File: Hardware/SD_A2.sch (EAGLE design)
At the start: 31 parts, among them IC1 74LS245N, IC2 LM317, IC3 2716 / 2732, IC4 XC9572XL

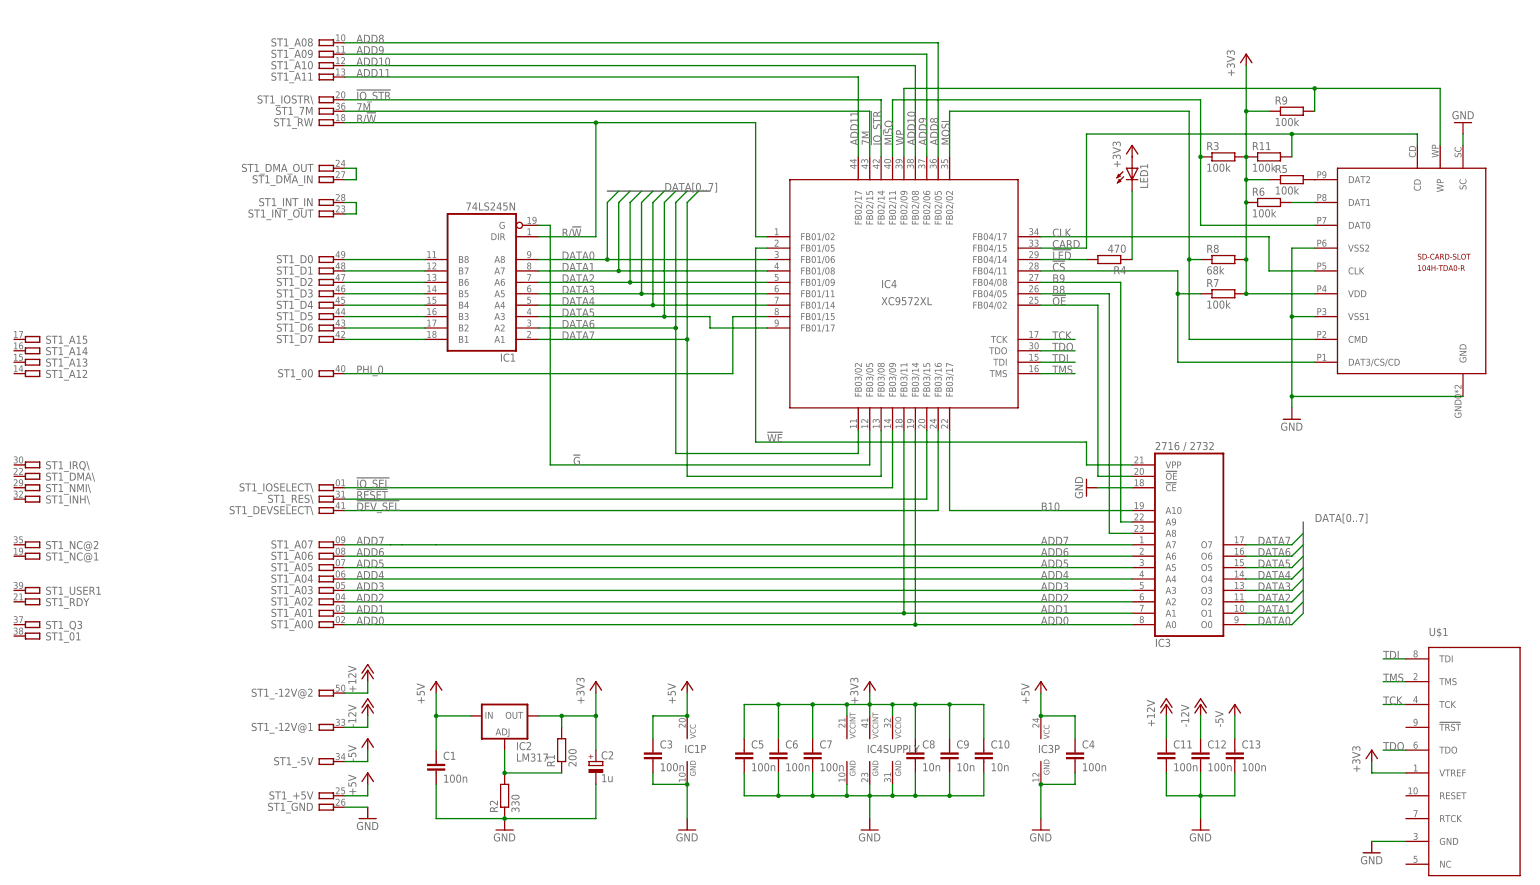
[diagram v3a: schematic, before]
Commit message: EEPROM as SMD
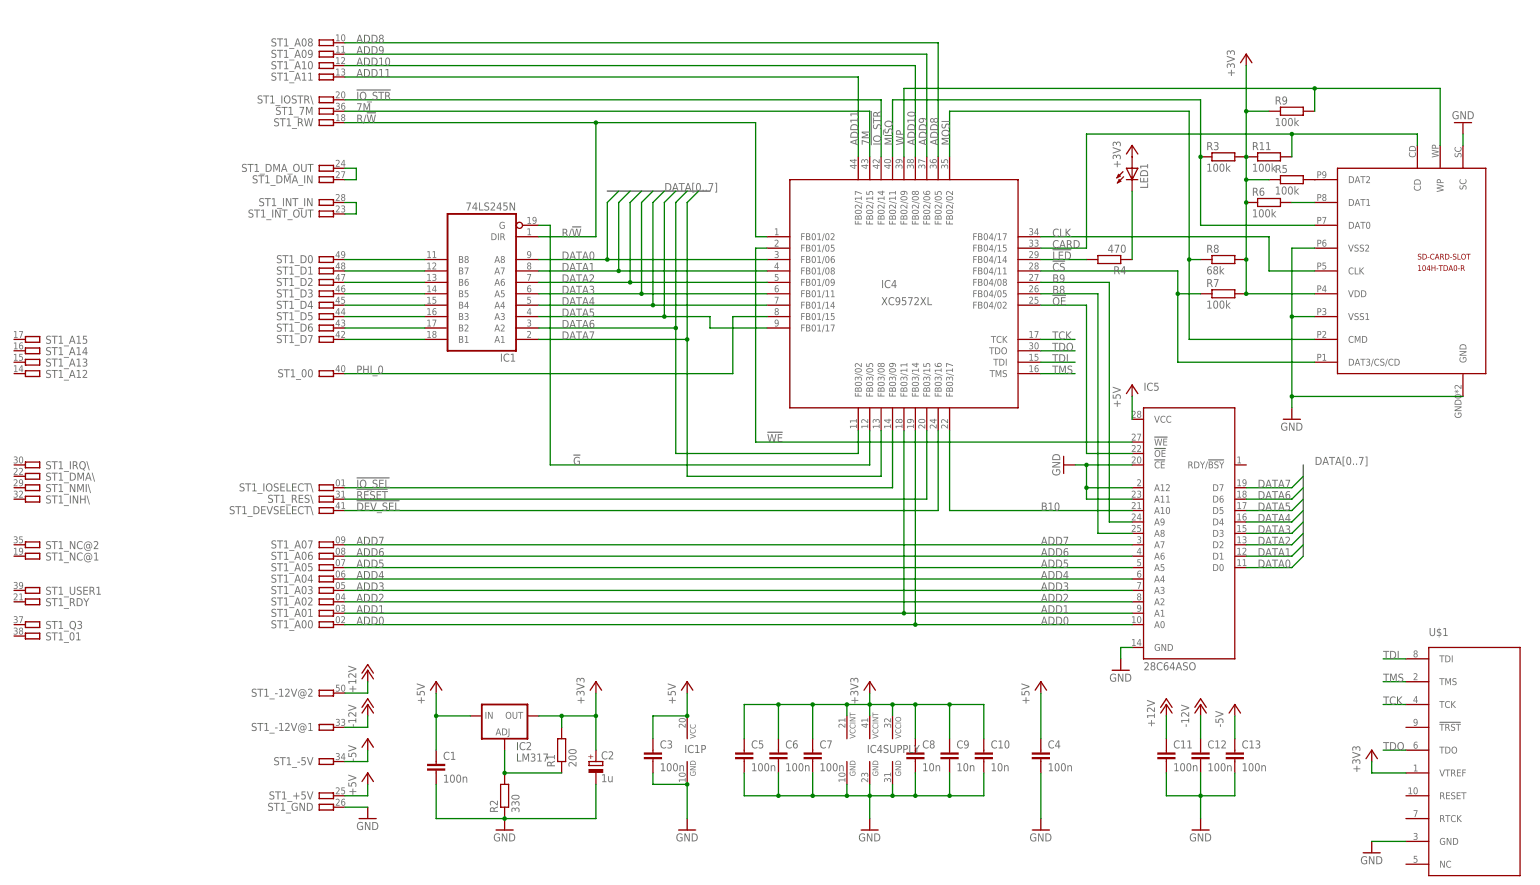
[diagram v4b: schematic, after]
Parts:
- removed IC3: 2716 / 2732, memory:2716
- added IC5: 28C64ASO, microchip:28C64ASO
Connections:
- net N$10 renamed D6
- net N$11 renamed D5
- net N$14 renamed D4
- net N$15 renamed D3
- net N$16 renamed D2
- net N$17 renamed D1
- net N$7 renamed D0
- net N$8 renamed D7
- net !OE: now also IC5.!OE; no longer IC3A.!OE
- net !WE: now also IC5.!WE; no longer IC3A.VPP
- net +5V: now also IC5.VCC; no longer IC3P.VCC
- net ADD0: now also IC5.A0; no longer IC3A.A0
- net ADD1: now also IC5.A1; no longer IC3A.A1
- net ADD2: now also IC5.A2; no longer IC3A.A2
- net ADD3: now also IC5.A3; no longer IC3A.A3
- net ADD4: now also IC5.A4; no longer IC3A.A4
- net ADD5: now also IC5.A5; no longer IC3A.A5
- net ADD6: now also IC5.A6; no longer IC3A.A6
- net ADD7: now also IC5.A7; no longer IC3A.A7
- net B10: now also IC5.A10; no longer IC3A.A10
- net B8: now also IC5.A8; no longer IC3A.A8
- net B9: now also IC5.A9; no longer IC3A.A9
- net DATA0: now also IC5.D0; no longer IC3A.O0
- net DATA1: now also IC5.D1; no longer IC3A.O1
- net DATA2: now also IC5.D2; no longer IC3A.O2
- net DATA3: now also IC5.D3; no longer IC3A.O3
- net DATA4: now also IC5.D4; no longer IC3A.O4
- net DATA5: now also IC5.D5; no longer IC3A.O5
- net DATA6: now also IC5.D6; no longer IC3A.O6
- net DATA7: now also IC5.D7; no longer IC3A.O7
- net GND: now also IC5.!CE, IC5.A11, IC5.A12, IC5.GND; no longer IC3A.!CE, IC3P.GND
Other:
- moved on the sheet: C4

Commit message: Resistor network added
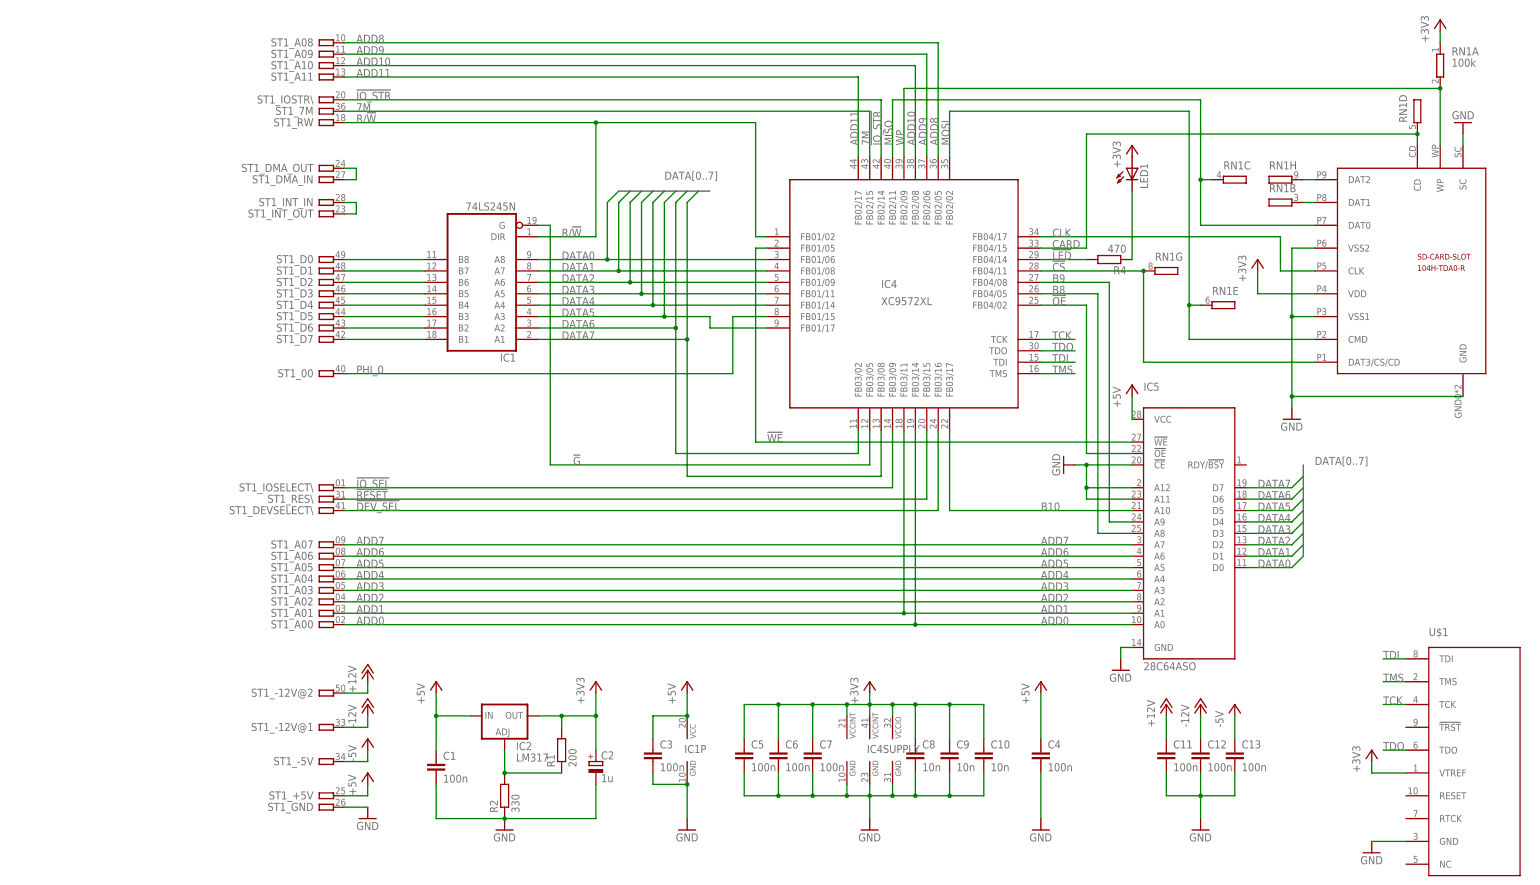
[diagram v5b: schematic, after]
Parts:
- removed R11, R3, R5, R6, R7, R9: 100k, rcl:R-EU_R0603
- removed R8: 68k, rcl:R-EU_R0603
- added RN1: 100k, resistor-sil:GE08R
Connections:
- removed net N$2: R5.2, U$2.DAT2
- removed net N$3: R6.2, U$2.DAT1
- new net DAT1: RN1B.2, U$2.DAT1
- new net DAT2: RN1H.2, U$2.DAT2
- net !CS: now also RN1G.2; no longer R7.1
- net +3V3: now also RN1A.1; no longer R11.1, R3.2, R5.1, R6.1, R7.2, R8.2, R9.1
- net CARD: now also RN1D.2; no longer R11.2
- net MISO: now also RN1C.2; no longer R3.1
- net MOSI: now also RN1E.2; no longer R8.1
- net WP: now also RN1A.2; no longer R9.2

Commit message: Trace width 0.254
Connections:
- net N$5 renamed DMA
- net N$6 renamed INT
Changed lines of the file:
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@@
 </segment>
 </net>
-<net name="N$5" class="0">
+<net name="DMA" class="0">
 <segment>
 <pinref part="ST1" gate="_DMA_OUT" pin="P"/>
@@
 </segment>
 </net>
-<net name="N$6" class="0">
+<net name="INT" class="0">
 <segment>
 <pinref part="ST1" gate="_INT_IN" pin="P"/>

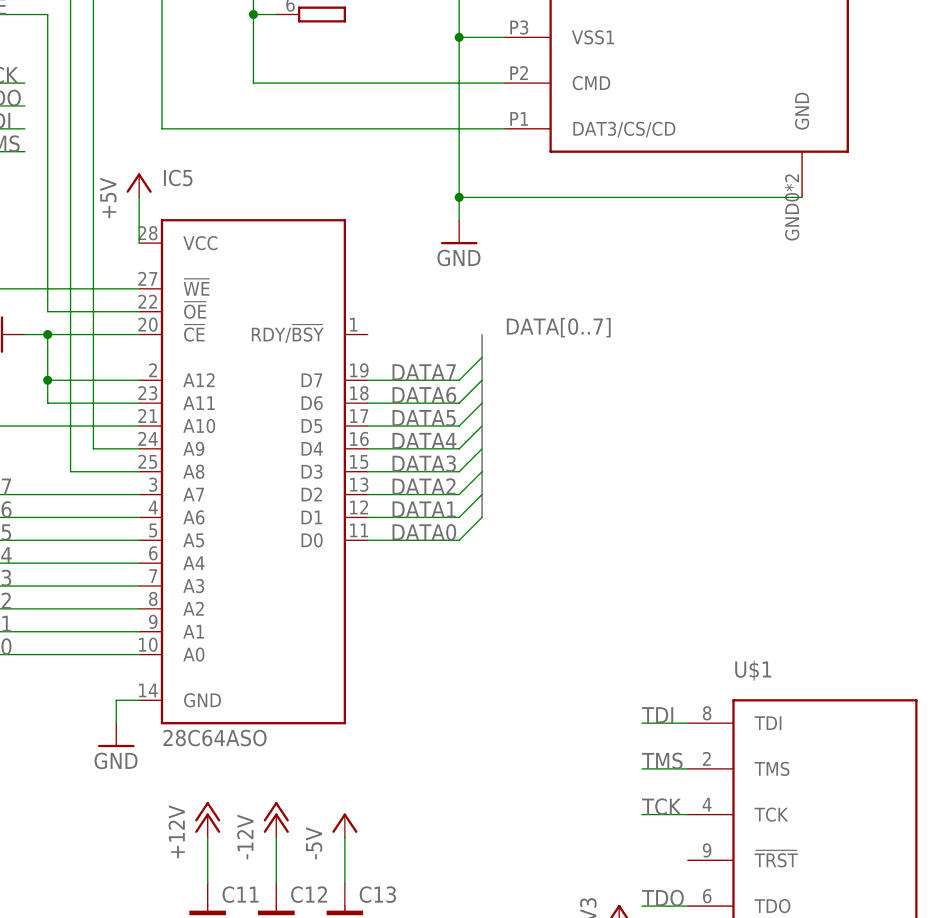
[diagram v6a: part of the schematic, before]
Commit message: Keepout for Tag Connect
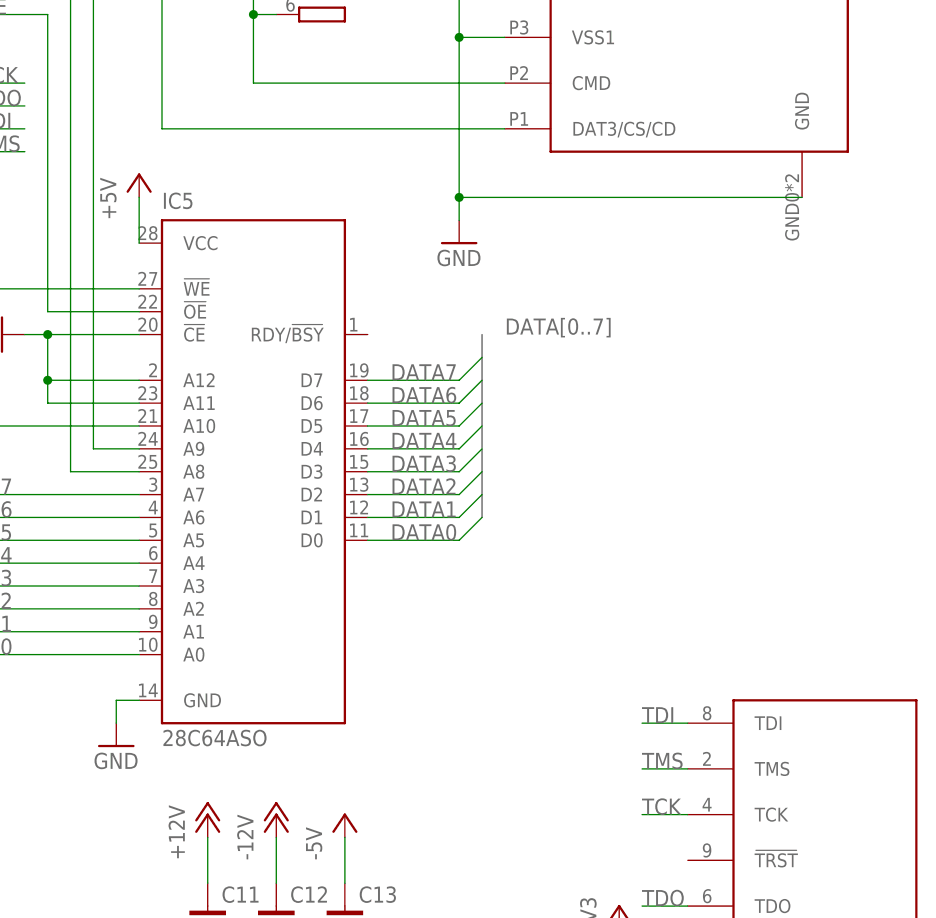
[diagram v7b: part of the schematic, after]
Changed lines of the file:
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@@
 <instance part="C12" gate="G$1" x="266.7" y="22.86"/>
 <instance part="C13" gate="G$1" x="274.32" y="22.86"/>
-<instance part="U$1" gate="G$1" x="330.2" y="30.48"/>
+<instance part="U$1" gate="G$1" x="330.2" y="30.48" smashed="yes"/>
 <instance part="+3V6" gate="G$1" x="304.8" y="22.86"/>
 <instance part="GND11" gate="1" x="304.8" y="0"/>
-<instance part="IC5" gate="G$1" x="264.16" y="73.66"/>
+<instance part="IC5" gate="G$1" x="264.16" y="73.66" smashed="yes">
+<attribute name="NAME" x="254" y="100.33" size="1.778" layer="95"/>
+<attribute name="VALUE" x="254" y="40.64" size="1.778" layer="96"/>
+</instance>
 <instance part="GND8" gate="1" x="248.92" y="40.64"/>
 <instance part="P+5" gate="1" x="251.46" y="104.14"/>
